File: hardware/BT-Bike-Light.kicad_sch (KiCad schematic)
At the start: 32 parts, among them J1 SWD_Header, J2 USB_C_Charge_Port, J3 BAT+, J4 BAT-, Q1 Q_NMOS_GDS, Q4 DSG/CHG, SW1 SW_Push, U1 BC805M, U2 LIS2DTW12, U3 PAM2808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

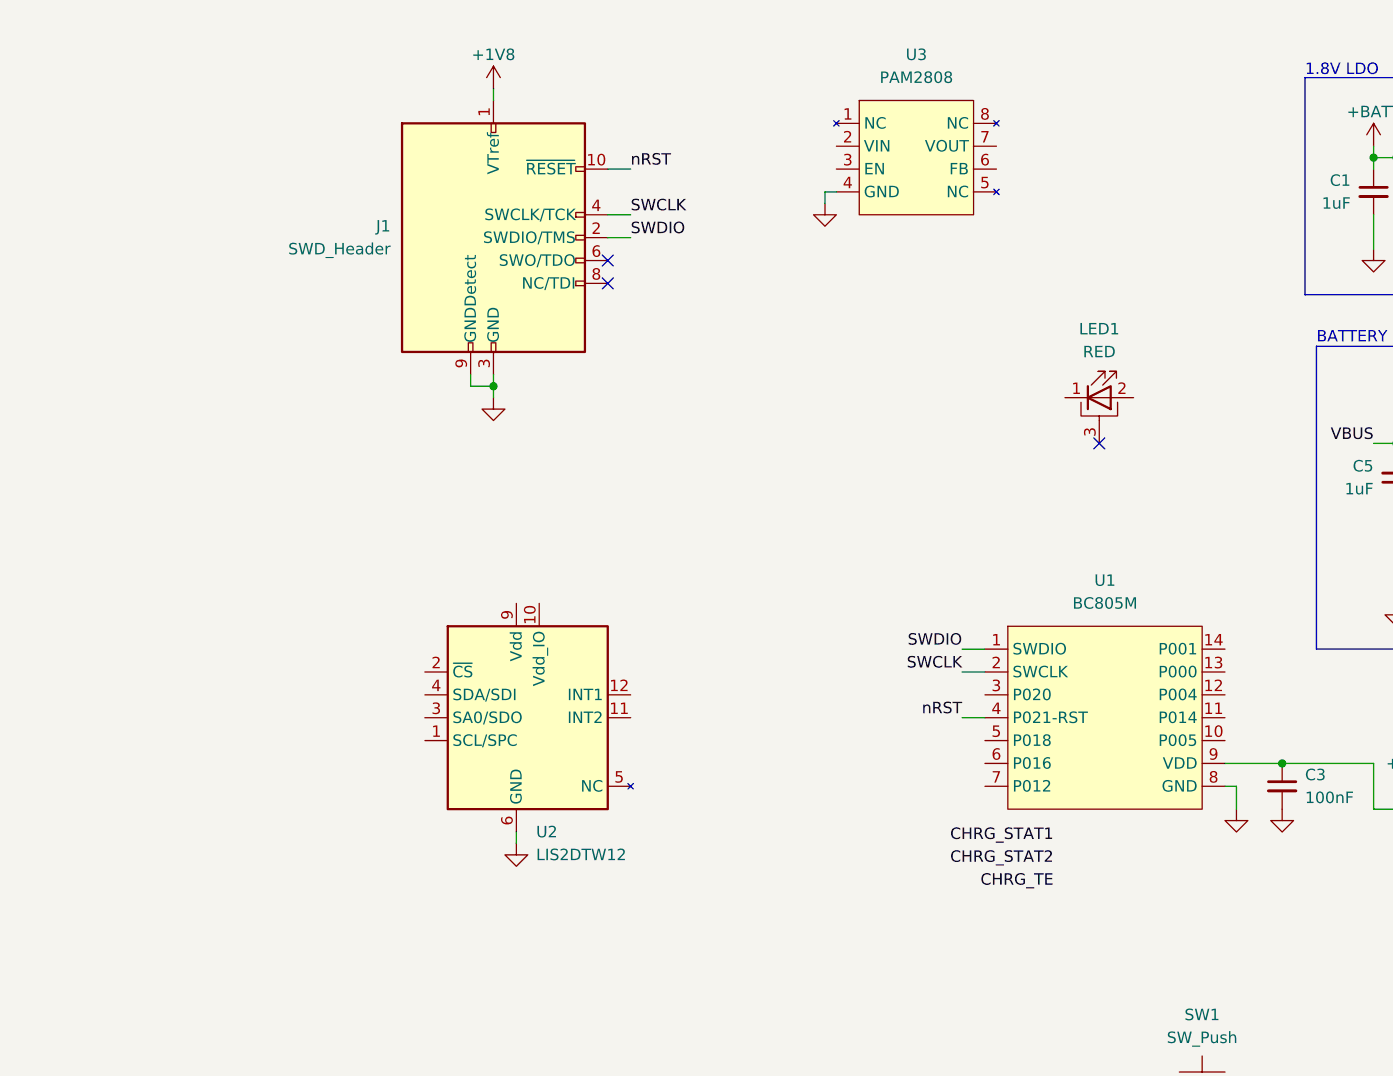
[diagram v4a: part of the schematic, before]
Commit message: Add supporting electronics for LED driver
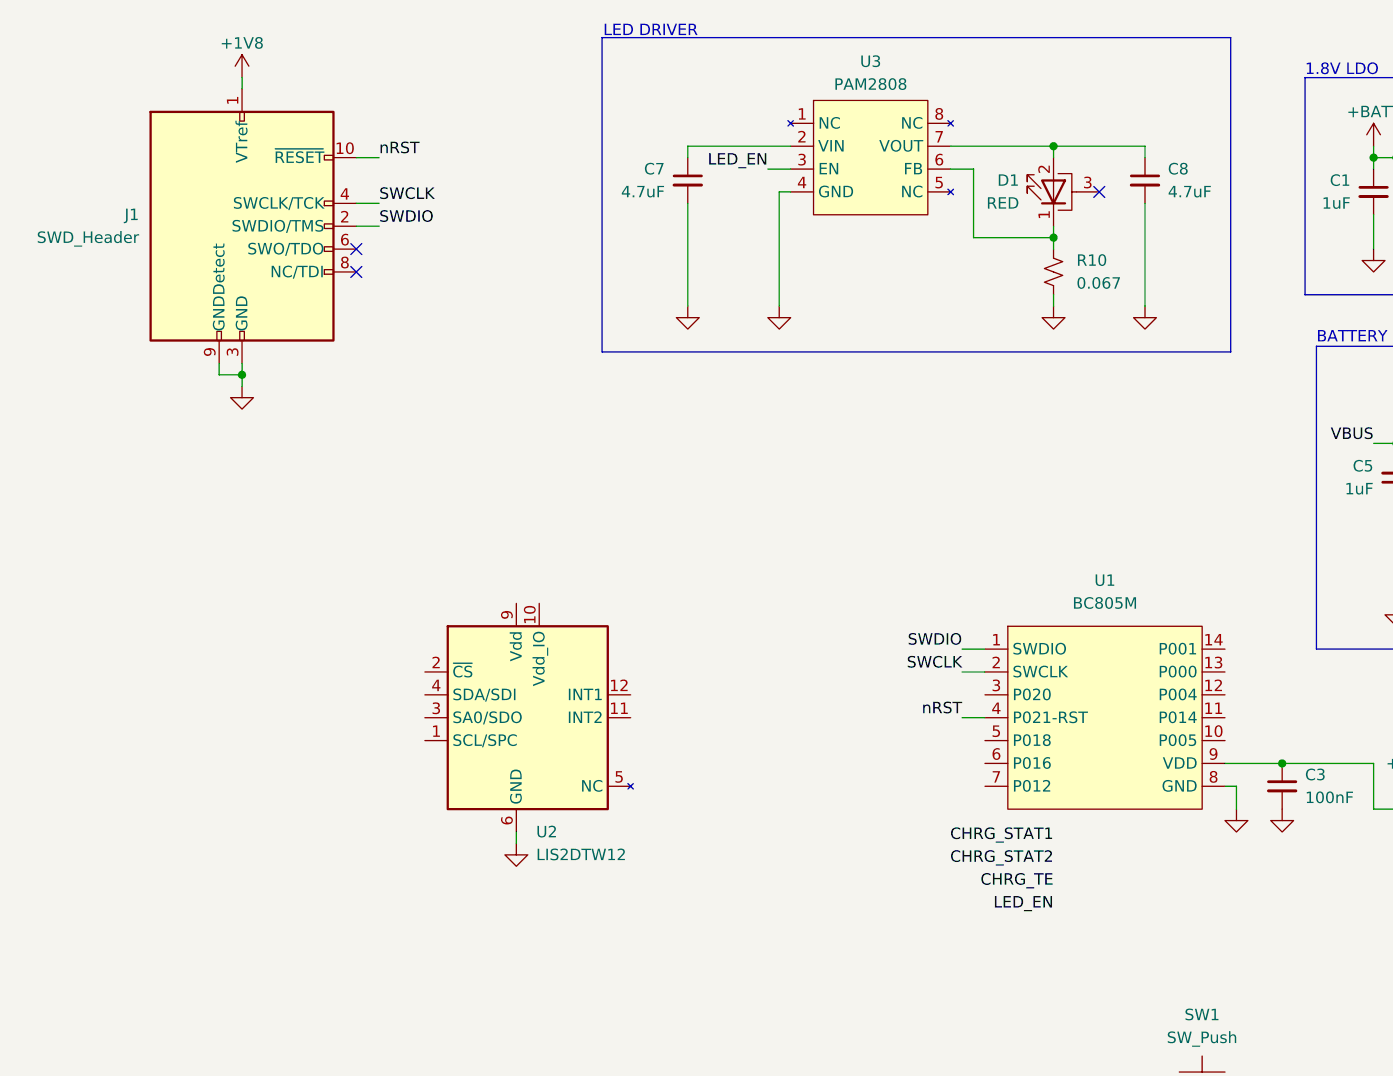
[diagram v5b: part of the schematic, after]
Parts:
- removed LED1: RED, LED_SMD:LED_Cree-XP, symbol Device:LED_Pad
- added C7, C8: 4.7uF, symbol Device:C_Small
- added D1: RED, LED_SMD:LED_Cree-XP, symbol Device:LED_Pad
- added R10: 0.067, symbol Device:R_Small_US
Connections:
- net GND: now also C7.2, C8.2, R10.1
- net at U3.2 (VIN): now also C7.1
- net LED_EN: now reaches U3.3 (EN)
- net at U3.6 (FB): now also D1.1 (K), R10.2
- net at U3.7 (VOUT): now also C8.1, D1.2 (A)
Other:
- note added: "LED DRIVER"
- moved on the sheet: J1, U3

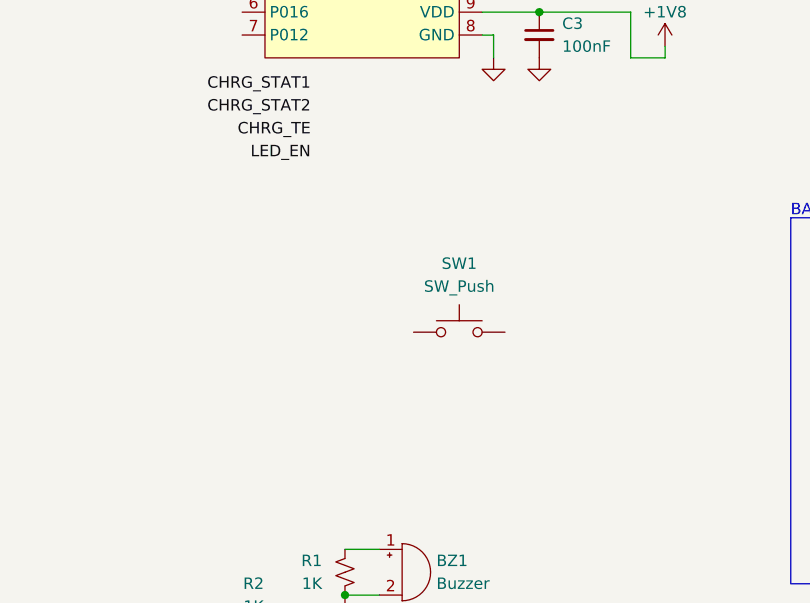
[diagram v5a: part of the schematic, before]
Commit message: Add supporting electronics for button
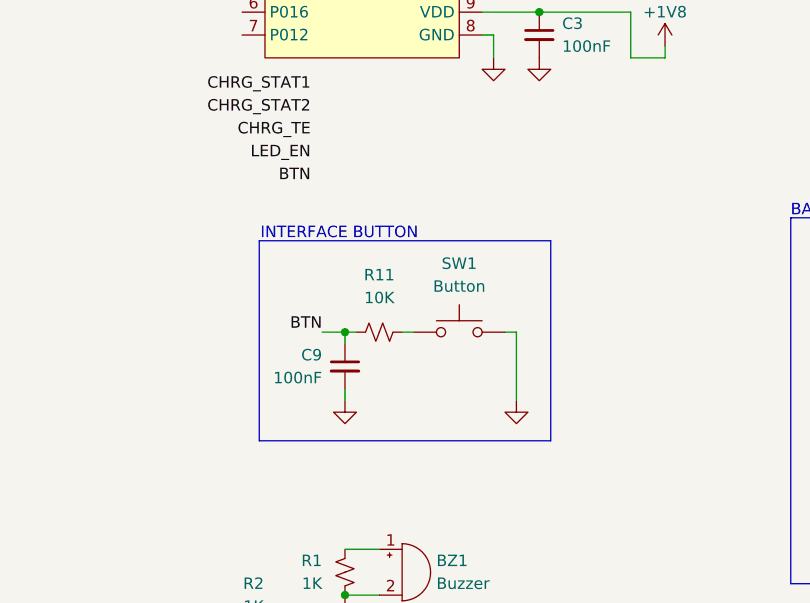
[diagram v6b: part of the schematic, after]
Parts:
- added C9: 100nF, symbol Device:C_Small
- added R11: 10K, symbol Device:R_Small_US
- SW1: value SW_Push -> Button
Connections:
- net GND: now also SW1.2, C9.2
- net at SW1.1: now also R11.2
- new net BTN: C9.1, R11.1
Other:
- note added: "INTERFACE BUTTON"

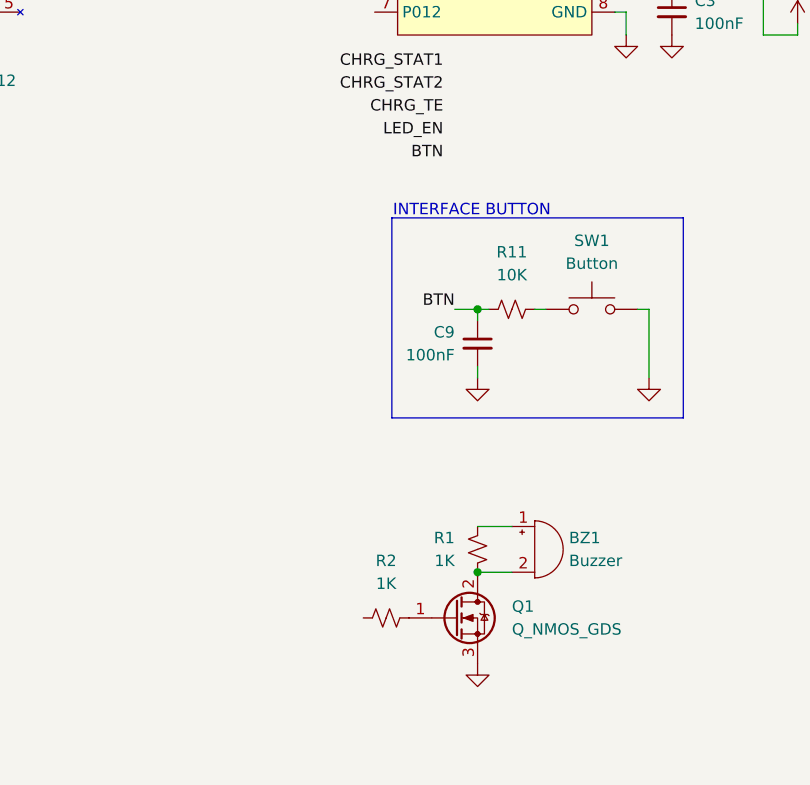
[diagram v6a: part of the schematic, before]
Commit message: Add supporting electronics for buzzer
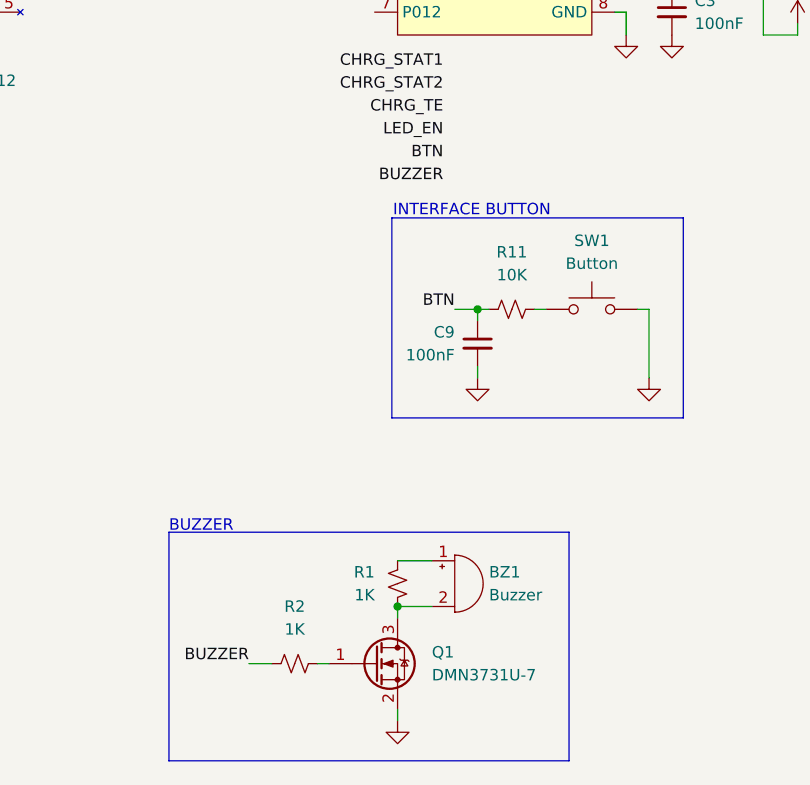
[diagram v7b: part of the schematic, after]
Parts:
- Q1: value Q_NMOS_GDS -> DMN3731U-7; footprint (none) -> Package_TO_SOT_SMD:SOT-23; symbol Device:Q_NMOS_GDS -> Device:Q_NMOS_GSD
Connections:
- net GND: now also Q1.2 (S); no longer Q1.3 (S)
- net BUZZER: now reaches R2.1
- net at BZ1.2 (-), R1.2: now also Q1.3 (D); no longer Q1.2 (D)
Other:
- note added: "BUZZER"
- moved on the sheet: BZ1, Q1, R1, R2
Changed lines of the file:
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@@
 	)
 	(junction
-		(at 138.43 170.18)
+		(at 129.54 173.99)
 		(diameter 0)
 		(color 0 0 0 0)
@@
 	(wire
 		(pts
+			(xy 129.54 175.26) (xy 129.54 173.99)
+		)
+		(stroke
+			(width 0)
+			(type default)
+		)
+	)
+	(wire
+		(pts
 			(xy 144.78 43.18) (xy 144.78 54.61)
 		)
@@
 	(wire
 		(pts
-			(xy 138.43 165.1) (xy 142.24 165.1)
+			(xy 129.54 168.91) (xy 133.35 168.91)
 		)
 		(stroke
@@
 	(wire
 		(pts
-			(xy 138.43 170.18) (xy 142.24 170.18)
+			(xy 129.54 173.99) (xy 133.35 173.99)
+		)
+		(stroke
+			(width 0)
+			(type default)
+		)
+	)
+	(wire
+		(pts
+			(xy 113.03 180.34) (xy 115.57 180.34)
 		)
 		(stroke
@@
 	(wire
 		(pts
+			(xy 129.54 185.42) (xy 129.54 186.69)
+		)
+		(stroke
+			(width 0)
+			(type default)
+		)
+	)
+	(wire
+		(pts
 			(xy 123.19 36.83) (xy 134.62 36.83)
 		)
@@
 	(wire
 		(pts
+			(xy 120.65 180.34) (xy 121.92 180.34)
+		)
+		(stroke
+			(width 0)
+			(type default)
+		)
+	)
+	(wire
+		(pts
 			(xy 58.42 184.15) (xy 58.42 189.23)
 		)
@@
 	)
 	(rectangle
+		(start 104.14 165.735)
+		(end 148.59 191.135)
+		(stroke
+			(width 0)
+			(type default)
+		)
+		(fill
+			(type none)
+		)
+	)
+	(rectangle
 		(start 162.56 29.21)
 		(end 208.28 53.34)
@@
 		)
 	)
+	(text "BUZZER"
+		(exclude_from_sim no)
+		(at 104.14 165.862 0)
+		(effects
+			(font
+				(size 1.27 1.27)
+			)
+			(justify left bottom)
+		)
+	)
 	(text "INTERFACE BUTTON"
 		(exclude_from_sim no)
@@
 		)
 	)
+	(label "BUZZER"
+		(at 113.03 180.34 180)
+		(fields_autoplaced yes)
+		(effects
+			(font
+				(size 1.27 1.27)
+			)
+			(justify right bottom)
+		)
+	)
 	(label "nRST"
 		(at 124.46 100.33 180)
@@
 		)
 	)
+	(label "BUZZER"
+		(at 134.62 127 180)
+		(fields_autoplaced yes)
+		(effects
+			(font
+				(size 1.27 1.27)
+			)
+			(justify right bottom)
+		)
+	)
 	(label "CHRG_STAT1"
 		(at 189.23 74.93 180)
@@
 	(symbol
 		(lib_id "Device:R_Small_US")
-		(at 128.27 175.26 90)
+		(at 118.11 180.34 90)
 		(unit 1)
 		(exclude_from_sim no)
@@
 		(fields_autoplaced yes)
 		(property "Reference" "R2"
-			(at 128.27 168.91 90)
+			(at 118.11 173.99 90)
 			(effects
 				(font
@@
 		)
 		(property "Value" "1K"
-			(at 128.27 171.45 90)
+			(at 118.11 176.53 90)
 			(effects
 				(font
@@
 		)
 		(property "Footprint" ""
-			(at 128.27 175.26 0)
+			(at 118.11 180.34 0)
 			(effects
 				(font
@@
 		)
 		(property "Datasheet" "~"
-			(at 128.27 175.26 0)
+			(at 118.11 180.34 0)
 			(effects
 				(font
@@
 		)
 		(property "Description" "Resistor, small US symbol"
-			(at 128.27 175.26 0)
+			(at 118.11 180.34 0)
 			(effects
 				(font
@@
 	)
 	(symbol
-		(lib_id "Device:Q_NMOS_GDS")
-		(at 135.89 175.26 0)
+		(lib_id "Device:Q_NMOS_GSD")
+		(at 127 180.34 0)
 		(unit 1)
 		(exclude_from_sim no)
@@
 		(fields_autoplaced yes)
 		(property "Reference" "Q1"
-			(at 142.24 173.9899 0)
+			(at 133.35 179.0699 0)
 			(effects
 				(font
@@
 			)
 		)
-		(property "Value" "Q_NMOS_GDS"
-			(at 142.24 176.5299 0)
+		(property "Value" "DMN3731U-7"
+			(at 133.35 181.6099 0)
 			(effects
 				(font
@@
 			)
 		)
-		(property "Footprint" ""
-			(at 140.97 172.72 0)
+		(property "Footprint" "Package_TO_SOT_SMD:SOT-23"
+			(at 132.08 177.8 0)
 			(effects
 				(font
@@
 			)
 		)
-		(property "Datasheet" "~"
-			(at 135.89 175.26 0)
+		(property "Datasheet" "https://www.diodes.com/assets/Datasheets/DMN3731U.pdf"
+			(at 127 180.34 0)
 			(effects
 				(font
@@
 			)
 		)
-		(property "Description" "N-MOSFET transistor, gate/drain/source"
-			(at 135.89 175.26 0)
+		(property "Description" "N-MOSFET transistor, gate/source/drain"
+			(at 127 180.34 0)
 			(effects
 				(font
@@
 	(symbol
 		(lib_id "power:GND")
-		(at 138.43 180.34 0)
+		(at 129.54 186.69 0)
 		(unit 1)
 		(exclude_from_sim no)
@@
 		(fields_autoplaced yes)
 		(property "Reference" "#PWR015"
-			(at 138.43 186.69 0)
+			(at 129.54 193.04 0)
 			(effects
 				(font
@@
 		)
 		(property "Value" "GND"
-			(at 138.43 185.42 0)
+			(at 129.54 191.77 0)
 			(effects
 				(font
@@
 		)
 		(property "Footprint" ""
-			(at 138.43 180.34 0)
+			(at 129.54 186.69 0)
 			(effects
 				(font
@@
 		)
 		(property "Datasheet" ""
-			(at 138.43 180.34 0)
+			(at 129.54 186.69 0)
 			(effects
 				(font
@@
 		)
 		(property "Description" "Power symbol creates a global label with name \"GND\" , ground"
-			(at 138.43 180.34 0)
+			(at 129.54 186.69 0)
 			(effects
 				(font
@@
 	(symbol
 		(lib_id "Device:Buzzer")
-		(at 144.78 167.64 0)
+		(at 135.89 171.45 0)
 		(unit 1)
 		(exclude_from_sim no)
@@
 		(fields_autoplaced yes)
 		(property "Reference" "BZ1"
-			(at 148.59 166.3699 0)
+			(at 139.7 170.1799 0)
 			(effects
 				(font
@@
 		)
 		(property "Value" "Buzzer"
-			(at 148.59 168.9099 0)
+			(at 139.7 172.7199 0)
 			(effects
 				(font
@@
 		)
 		(property "Footprint" "PUI-Audio:PUI_AT-1220-TT-3V-2-R"
-			(at 144.145 165.1 90)
+			(at 135.255 168.91 90)
 			(effects
 				(font
@@
 		)
 		(property "Datasheet" "https://api.puiaudio.com/file/cb716568-5258-4e08-b27f-2aa736c8b20d.pdf"
-			(at 144.145 165.1 90)
+			(at 135.255 168.91 90)
 			(effects
 				(font
@@
 		)
 		(property "Description" "Buzzer, polarized"
-			(at 144.78 167.64 0)
+			(at 135.89 171.45 0)
 			(effects
 				(font
@@
 	(symbol
 		(lib_id "Device:R_Small_US")
-		(at 138.43 167.64 0)
+		(at 129.54 171.45 0)
 		(mirror y)
 		(unit 1)
@@
 		(dnp no)
 		(property "Reference" "R1"
-			(at 135.89 166.3699 0)
+			(at 127 170.1799 0)
 			(effects
 				(font
@@
 		)
 		(property "Value" "1K"
-			(at 135.89 168.9099 0)
+			(at 127 172.7199 0)
 			(effects
 				(font
@@
 		)
 		(property "Footprint" ""
-			(at 138.43 167.64 0)
+			(at 129.54 171.45 0)
 			(effects
 				(font
@@
 		)
 		(property "Datasheet" "~"
-			(at 138.43 167.64 0)
+			(at 129.54 171.45 0)
 			(effects
 				(font
@@
 		)
 		(property "Description" "Resistor, small US symbol"
-			(at 138.43 167.64 0)
+			(at 129.54 171.45 0)
 			(effects
 				(font

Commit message: Add supporting electronics for accelerometer
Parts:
- added C10, C12: 100nF, symbol Device:C_Small
- added C11: 10uF, symbol Device:C_Small
- added JP1: TIM_DISABLE, symbol Jumper:Jumper_2_Open
- added R12, R13, R14: 10K, symbol Device:R_Small_US
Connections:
- net +1V8: now also U2.10 (Vdd_IO), U2.2 (~{CS}), U2.9 (Vdd), C10.1, C11.1, C12.1, R12.1, R13.1
- net CHRG_TE: now also JP1.1 (A), R14.1
- net GND: now also C10.2, C11.2, C12.2, R14.2
- net VBUS: now also JP1.2 (B)
- net SCL: now reaches U2.1 (SCL/SPC)
- net SCL: now also R12.2
- net ACCEL_INT2: now reaches U2.11 (INT2)
- net ACCEL_INT1: now reaches U2.12 (INT1)
- net SDA: now reaches U2.4 (SDA/SDI)
- net SDA: now also R13.2
- no-connect marks 3 -> 4
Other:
- note added: "ACCELEROMETER"
